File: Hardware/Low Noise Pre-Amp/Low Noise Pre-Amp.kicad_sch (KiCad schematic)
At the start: 53 parts, among them J1 RF2-152-T-00-50-G-HDW, J2 RF2-152-T-00-50-G-HDW, J3 RF2-152-T-00-50-G-HDW, U1 ADA4841-2, U2 ADA4841-2, U3 LTC3260xMSE, U4 L78L05_SOT89, U5 L79L05

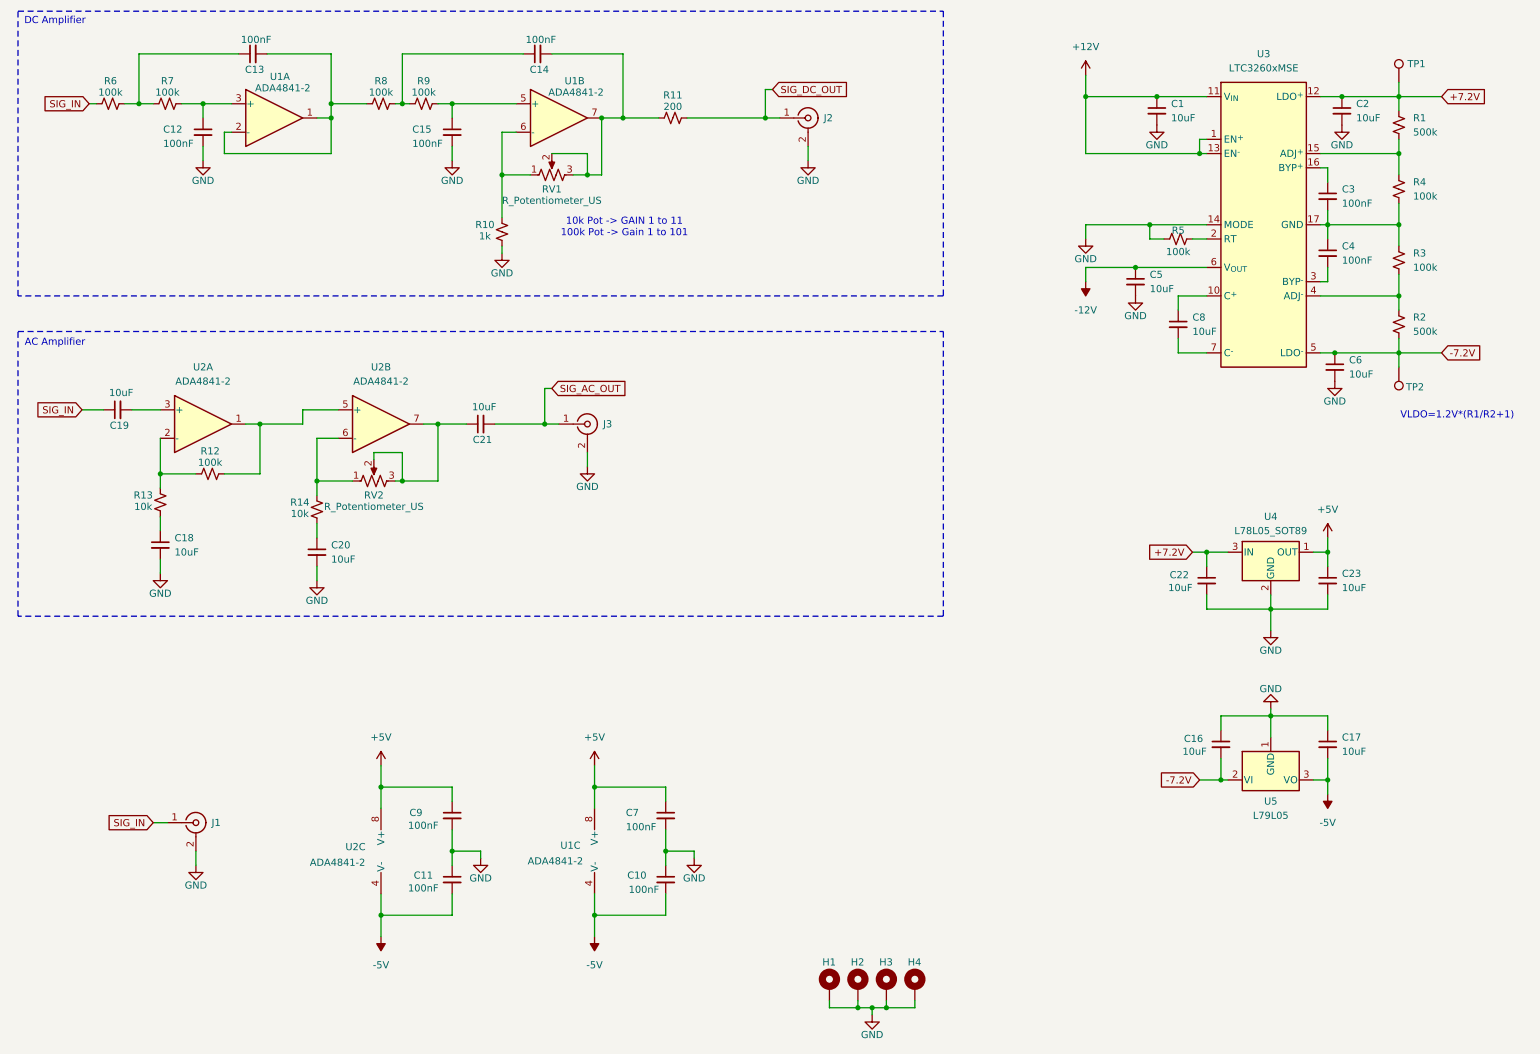
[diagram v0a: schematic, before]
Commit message: Adding Low Noise Pre-Amp board
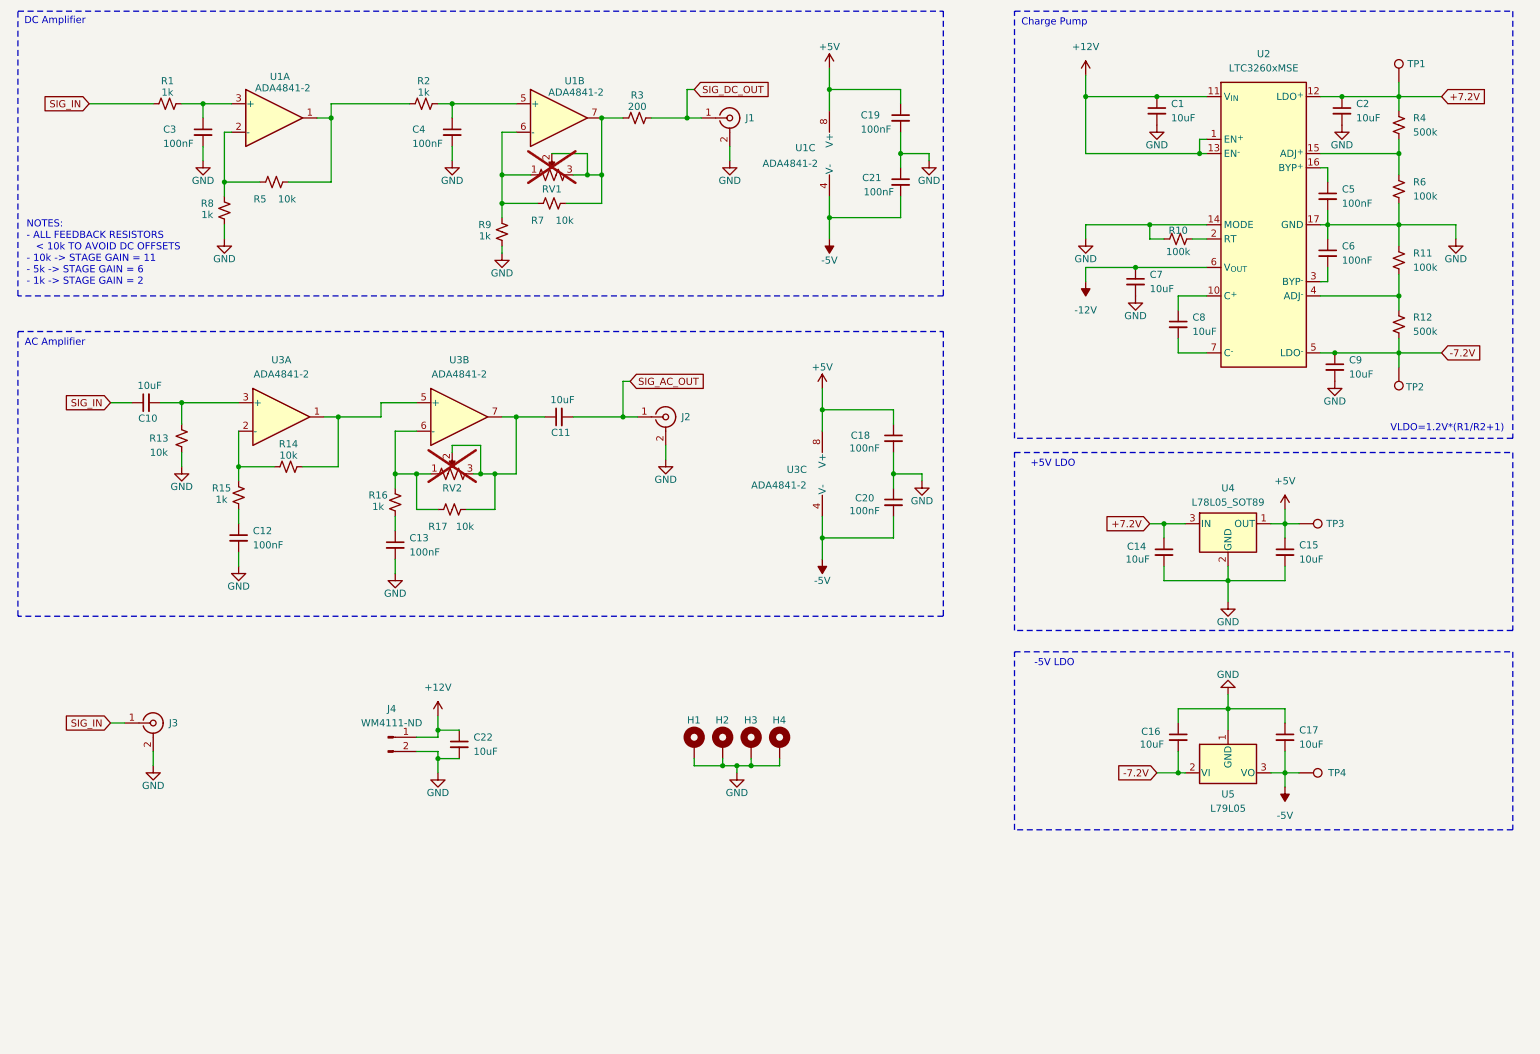
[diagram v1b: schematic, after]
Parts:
- removed C13, C14: 100nF, symbol Device:C_Small
- removed R6: 100k, symbol Device:R_Small_US
- added C22: 10uF, Capacitor_SMD:C_0805_2012Metric, symbol Device:C_Small
- added J4: WM4111-ND, Connector_Molex:Molex_KK-254_AE-6410-02A_1x02_P2.54mm_Vertical, symbol Connector:Conn_01x02_Pin
- added R13, R17, R5, R7: 10k, Resistor_SMD:R_0805_2012Metric, symbol Device:R_Small_US
- added TP3, TP4: TestPoint, TestPoint:TestPoint_Pad_D1.0mm, symbol Connector:TestPoint
- C1, C16, C17, C2, C8: footprint (none) -> Capacitor_SMD:C_0805_2012Metric
- C10: renamed from C19; footprint (none) -> Capacitor_SMD:C_0805_2012Metric
- C11: renamed from C21; footprint (none) -> Capacitor_SMD:C_0805_2012Metric
- C12: renamed from C18; value 10uF -> 100nF; footprint (none) -> Capacitor_SMD:C_0805_2012Metric
- C13: renamed from C20; value 10uF -> 100nF; footprint (none) -> Capacitor_SMD:C_0805_2012Metric
- C14: renamed from C22; footprint (none) -> Capacitor_SMD:C_0805_2012Metric
- C15: renamed from C23; footprint (none) -> Capacitor_SMD:C_0805_2012Metric
- C18: renamed from C9; footprint (none) -> Capacitor_SMD:C_0805_2012Metric
- C19: renamed from C7; footprint (none) -> Capacitor_SMD:C_0805_2012Metric
- C20: renamed from C11; footprint (none) -> Capacitor_SMD:C_0805_2012Metric
- C21: renamed from C10; footprint (none) -> Capacitor_SMD:C_0805_2012Metric
- C3: renamed from C12; footprint (none) -> Capacitor_SMD:C_0805_2012Metric
- C4: renamed from C15; footprint (none) -> Capacitor_SMD:C_0805_2012Metric
- C5: renamed from C3; footprint (none) -> Capacitor_SMD:C_0805_2012Metric
- C6: renamed from C4; footprint (none) -> Capacitor_SMD:C_0805_2012Metric
- C7: renamed from C5; footprint (none) -> Capacitor_SMD:C_0805_2012Metric
- C9: renamed from C6; footprint (none) -> Capacitor_SMD:C_0805_2012Metric
- H1, H2, H3, H4: footprint (none) -> MountingHole:MountingHole_3.2mm_M3_DIN965_Pad
- J1: renamed from J2; footprint (none) -> Connector_Coaxial:SMA_Wurth_60312002114503_Vertical
- J2: renamed from J3; footprint (none) -> Connector_Coaxial:SMA_Wurth_60312002114503_Vertical
- J3: renamed from J1; footprint (none) -> Connector_Coaxial:SMA_Wurth_60312002114503_Vertical
- R1: renamed from R7; value 100k -> 1k; footprint (none) -> Resistor_SMD:R_0805_2012Metric
- R10: renamed from R5; footprint (none) -> Resistor_SMD:R_0805_2012Metric
- R11: renamed from R3; footprint (none) -> Resistor_SMD:R_0805_2012Metric
- R12: renamed from R2; footprint (none) -> Resistor_SMD:R_0805_2012Metric
- R14: renamed from R12; value 100k -> 10k; footprint (none) -> Resistor_SMD:R_0805_2012Metric
- R15: renamed from R13; value 10k -> 1k; footprint (none) -> Resistor_SMD:R_0805_2012Metric
- R16: renamed from R14; value 10k -> 1k; footprint (none) -> Resistor_SMD:R_0805_2012Metric
- R2: renamed from R9; value 100k -> 1k; footprint (none) -> Resistor_SMD:R_0805_2012Metric
- R3: renamed from R11; footprint (none) -> Resistor_SMD:R_0805_2012Metric
- R4: renamed from R1; footprint (none) -> Resistor_SMD:R_0805_2012Metric
- R6: renamed from R4; footprint (none) -> Resistor_SMD:R_0805_2012Metric
- R8: value 100k -> 1k; footprint (none) -> Resistor_SMD:R_0805_2012Metric
- R9: renamed from R10; footprint (none) -> Resistor_SMD:R_0805_2012Metric
- RV1, RV2: footprint (none) -> Connector_PinHeader_2.54mm:PinHeader_1x03_P2.54mm_Vertical; now not fitted
- TP1, TP2: footprint (none) -> TestPoint:TestPoint_Pad_D1.0mm
- renumbered U3 to U2, U2 to U3
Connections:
- net +12V: now also C22.1, J4.1 (Pin_1)
- net +5V: now also TP3.1
- net -5V: now also TP4.1
- net GND: now also C5.2, C6.1, R11.1, R6.2, R8.1, U2.17 (GND), C22.2, J4.2 (Pin_2), R13.1
- net SIG_IN: now also R1.1
- net at R16.2, RV2.1, U3.6 (-): now also R17.2
- net at C11.1, RV2.2, RV2.3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: now also R17.1
- net at C10.2, U3.3 (+): now also R13.2
- net at R8.2: now also U1.2 (-), R5.2; no longer R2.1
- net at R3.1, RV1.2, RV1.3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: now also R7.1
- net at R9.2, RV1.1, U1.6 (-): now also R7.2
- new net: R2.1, R5.1, U1.1
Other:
- note added: "+5V LDO"
- note added: "-5V LDO"
- note added: "Charge Pump"
- note added: "NOTES: - ALL FEEDBACK RESISTORS < 10k TO AVOID DC OFFSETS - 10k -> STAGE GAIN = 11 - 5k -> STAGE GAIN = 6 - 1k -> STAGE GAIN = 2"
- note removed: "10k Pot -> GAIN 1 to 11 100k Pot -> Gain 1 to 101"
- moved on the sheet: C10, C11, C12, C13, C14, C15, C16, C17, C18, C19, C20, C21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

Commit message: Minor changes to Pre amp
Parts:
- removed H3: M3, MountingHole:MountingHole_3.2mm_M3_DIN965_Pad, symbol Mechanical:MountingHole_Pad
- C1, C2, C22: Digikey (none) -> 490-18663-1-ND; MPN (none) -> GRM21BR61H106KE43L; Manufacturer (none) -> Murata Electronics
- C10: renamed from C8; Digikey (none) -> 490-18663-1-ND; MPN (none) -> GRM21BR61H106KE43L; Manufacturer (none) -> Murata Electronics
- C11: renamed from C9; Digikey (none) -> 490-18663-1-ND; MPN (none) -> GRM21BR61H106KE43L; Manufacturer (none) -> Murata Electronics
- C12: renamed from C10; Digikey (none) -> 490-18663-1-ND; MPN (none) -> GRM21BR61H106KE43L; Manufacturer (none) -> Murata Electronics
- C13: renamed from C11; Digikey (none) -> 490-18663-1-ND; MPN (none) -> GRM21BR61H106KE43L; Manufacturer (none) -> Murata Electronics
- C14: renamed from C18; Digikey (none) -> 399-C0805C104K5RACTUCT-ND; MPN (none) -> C0805C104K5RACTU; Manufacturer (none) -> KEMET
- C15: renamed from C20; Digikey (none) -> 399-C0805C104K5RACTUCT-ND; MPN (none) -> C0805C104K5RACTU; Manufacturer (none) -> KEMET
- C16: renamed from C12; Digikey (none) -> 399-C0805C104K5RACTUCT-ND; MPN (none) -> C0805C104K5RACTU; Manufacturer (none) -> KEMET
- C17: renamed from C13; Digikey (none) -> 399-C0805C104K5RACTUCT-ND; MPN (none) -> C0805C104K5RACTU; Manufacturer (none) -> KEMET
- C18: renamed from C14; Digikey (none) -> 490-18663-1-ND; MPN (none) -> GRM21BR61H106KE43L; Manufacturer (none) -> Murata Electronics
- C19: renamed from C15; Digikey (none) -> 490-18663-1-ND; MPN (none) -> GRM21BR61H106KE43L; Manufacturer (none) -> Murata Electronics
- C20: renamed from C16; Digikey (none) -> 490-18663-1-ND; MPN (none) -> GRM21BR61H106KE43L; Manufacturer (none) -> Murata Electronics
- C21: renamed from C17; Digikey (none) -> 490-18663-1-ND; MPN (none) -> GRM21BR61H106KE43L; Manufacturer (none) -> Murata Electronics
- C3: renamed from C19; Digikey (none) -> 399-C0805C104K5RACTUCT-ND; MPN (none) -> C0805C104K5RACTU; Manufacturer (none) -> KEMET
- C4: renamed from C3; Digikey (none) -> 399-C0805C104K5RACTUCT-ND; MPN (none) -> C0805C104K5RACTU; Manufacturer (none) -> KEMET
- C5: renamed from C4; Digikey (none) -> 399-C0805C104K5RACTUCT-ND; MPN (none) -> C0805C104K5RACTU; Manufacturer (none) -> KEMET
- C6: renamed from C21; Digikey (none) -> 399-C0805C104K5RACTUCT-ND; MPN (none) -> C0805C104K5RACTU; Manufacturer (none) -> KEMET
- C7: renamed from C5; Digikey (none) -> 399-C0805C104K5RACTUCT-ND; MPN (none) -> C0805C104K5RACTU; Manufacturer (none) -> KEMET
- C8: renamed from C6; Digikey (none) -> 399-C0805C104K5RACTUCT-ND; MPN (none) -> C0805C104K5RACTU; Manufacturer (none) -> KEMET
- C9: renamed from C7; Digikey (none) -> 490-18663-1-ND; MPN (none) -> GRM21BR61H106KE43L; Manufacturer (none) -> Murata Electronics
- R1, R15, R16, R2, R8, R9: Digikey (none) -> 311-1.00KCRCT-ND; MPN (none) -> RC0805FR-071KL; Manufacturer (none) -> YAGEO
- R10, R11, R6: Digikey (none) -> 311-100KCRCT-ND; MPN (none) -> RC0805FR-07100KL; Manufacturer (none) -> YAGEO
- R12, R4: value 500k -> 510k; Digikey (none) -> 13-RC0805FR-13510KLCT-ND; MPN (none) -> RC0805FR-13510KL; Manufacturer (none) -> YAGEO
- R13, R14, R17, R5, R7: Digikey (none) -> 311-10.0KCRCT-ND; MPN (none) -> RC0805FR-0710KL; Manufacturer (none) -> YAGEO
- R3: value 200 -> 220; Digikey (none) -> 311-220CRCT-ND; MPN (none) -> RC0805FR-07220RL; Manufacturer (none) -> YAGEO
- renumbered H4 to H3
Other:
- moved on the sheet: H3

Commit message: adding script to sweep frequency and phase while tuning
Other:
- note added: "Future Improvements: For DC Amplifier Use OPA2990, with gain of ~22 For AC Amplifier User ADA4898, for lower noise"
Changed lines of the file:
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@@
+		)
+	)
+	(text "Future Improvements:\nFor DC Amplifier Use OPA2990, with gain of ~22\nFor AC Amplifier User ADA4898, for lower noise"
+		(exclude_from_sim no)
+		(at 17.018 191.008 0)
+		(effects
+			(font
+				(size 1.27 1.27)
+			)
+			(justify left)
 		)
 	)
